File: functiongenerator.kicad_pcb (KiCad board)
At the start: 2 copper layers, 100 x 71 mm, 59 parts, among them J1 Conn_01x02_Socket, J2 Amplitude, J3 Amplitude, J4 offset, J5 offset, U1 LM6172, U2 LM6172, X1 CON1, X2 CON2

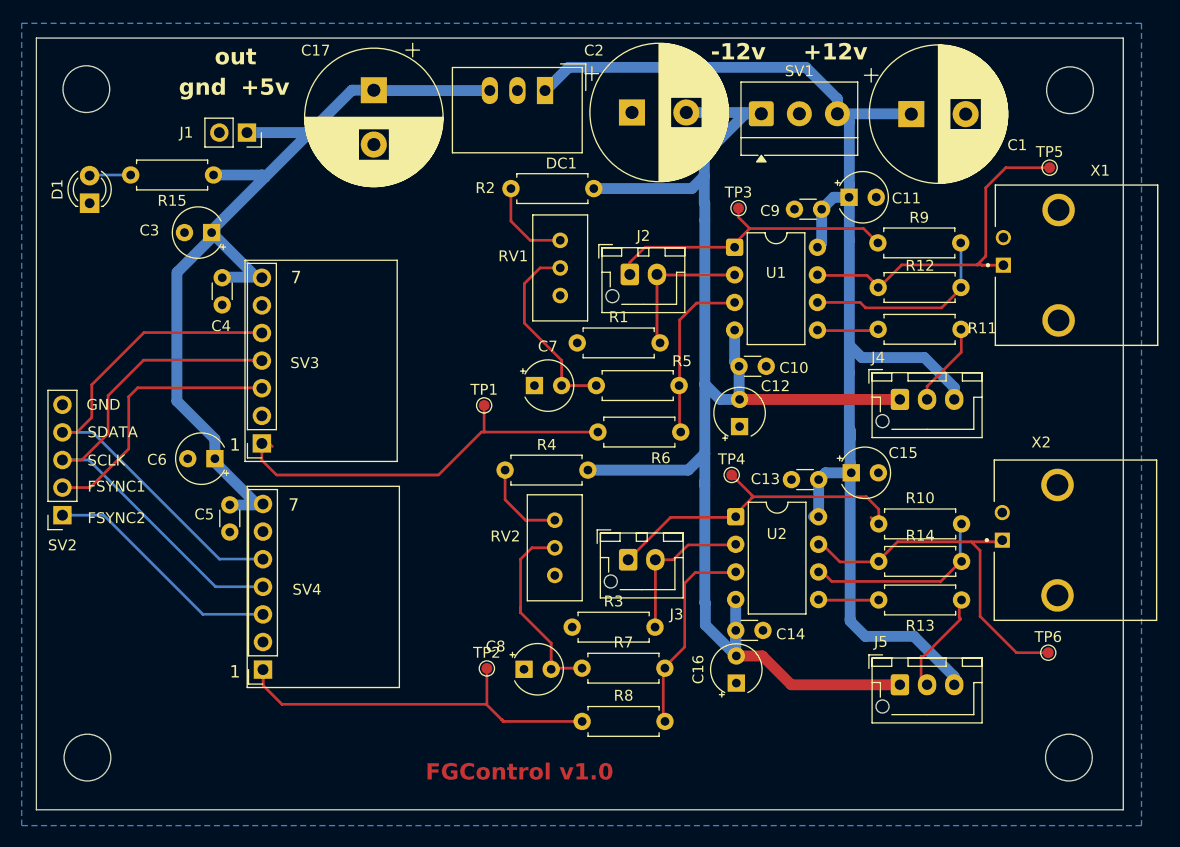
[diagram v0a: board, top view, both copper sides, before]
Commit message: first cleanup groundplane
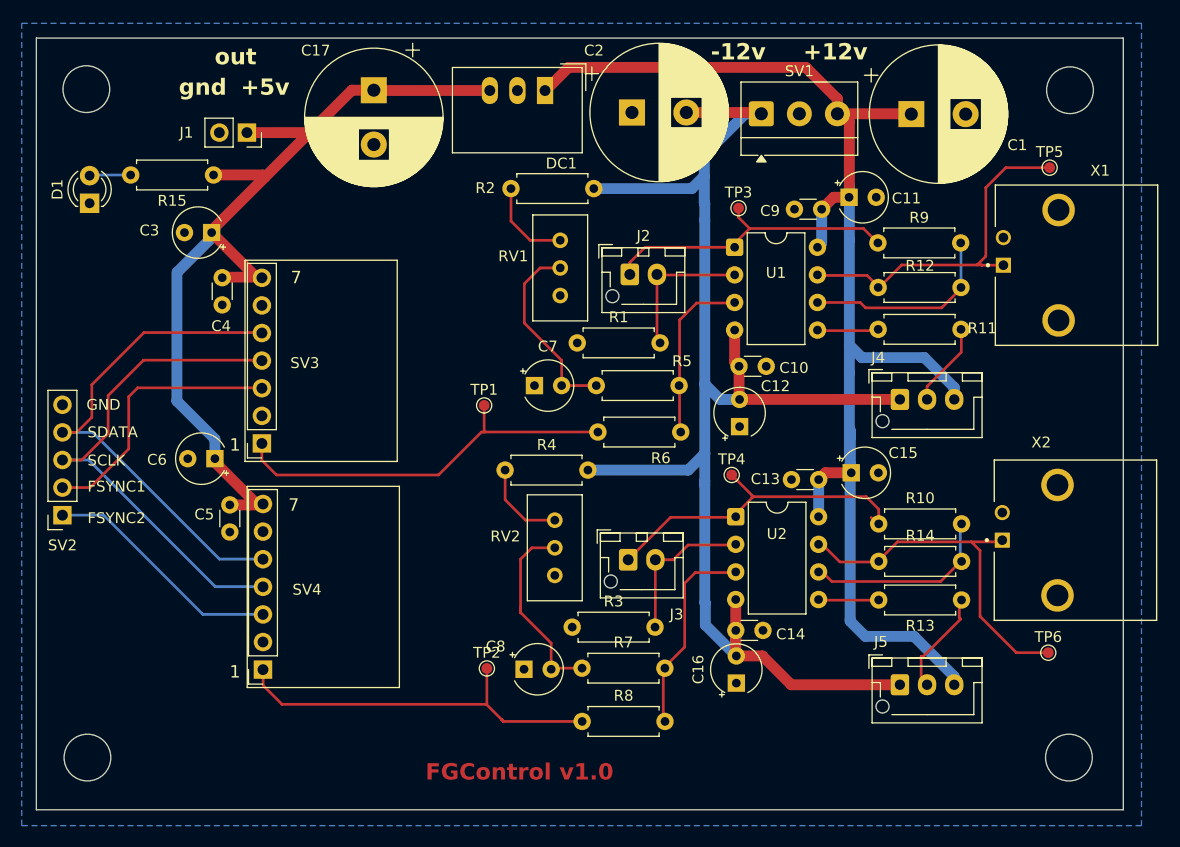
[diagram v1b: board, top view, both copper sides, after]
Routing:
- net /+12v: track 126.9 -> 131.7 mm
- net /+5v: track 84.5 -> 86.3 mm
- net Net-(SV3-Pin_1): track 38.1 -> 37.1 mm
- net /-12v: track 130.8 -> 131.4 mm

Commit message: moved offset potmeter connections
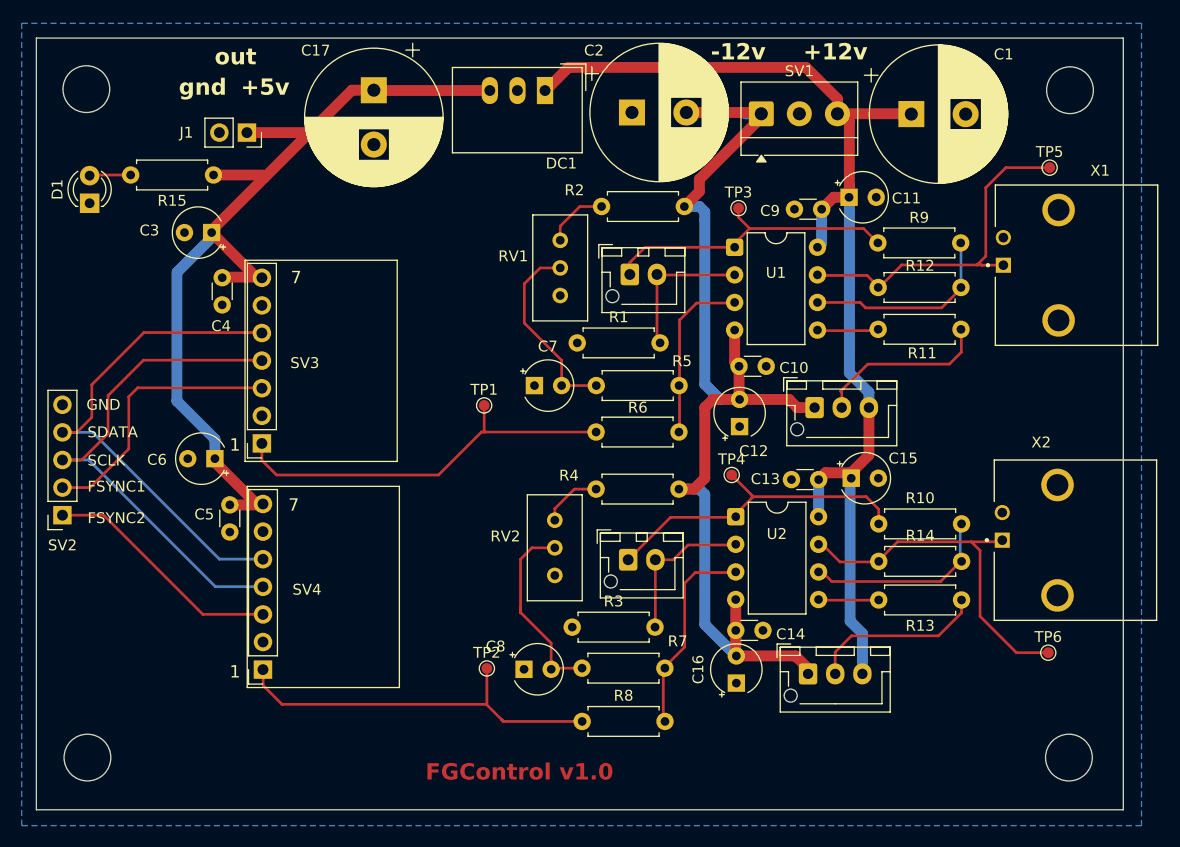
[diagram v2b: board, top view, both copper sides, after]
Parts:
- moved R4 8.56 mm to (157.6, 111.0)
- moved J5 8.51 mm to (169.5, 128.0)
- moved R2 8.50 mm to (158.1, 85.0)
- moved J4 7.89 mm to (170.1, 103.5)
- moved C15 0.50 mm to (173.5, 110.0)
- moved R6 0.16 mm to (150.0, 105.8)
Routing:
- net /-12v: track 131.4 -> 101.4 mm
- net /+12v: track 131.7 -> 109.7 mm
- net Net-(J4-Pin_2): track 7.57 -> 16.1 mm
- net Net-(J5-Pin_2): track 9.59 -> 16.3 mm
- net Net-(R4-Pad2): track 8.08 -> 5.61 mm
- net Net-(R2-Pad2): track 8.26 -> 5.86 mm
- net /+5v: track 86.3 -> 85.2 mm
- net Net-(J3-Pin_1): track 31.5 -> 30.7 mm

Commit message: removed exces traces
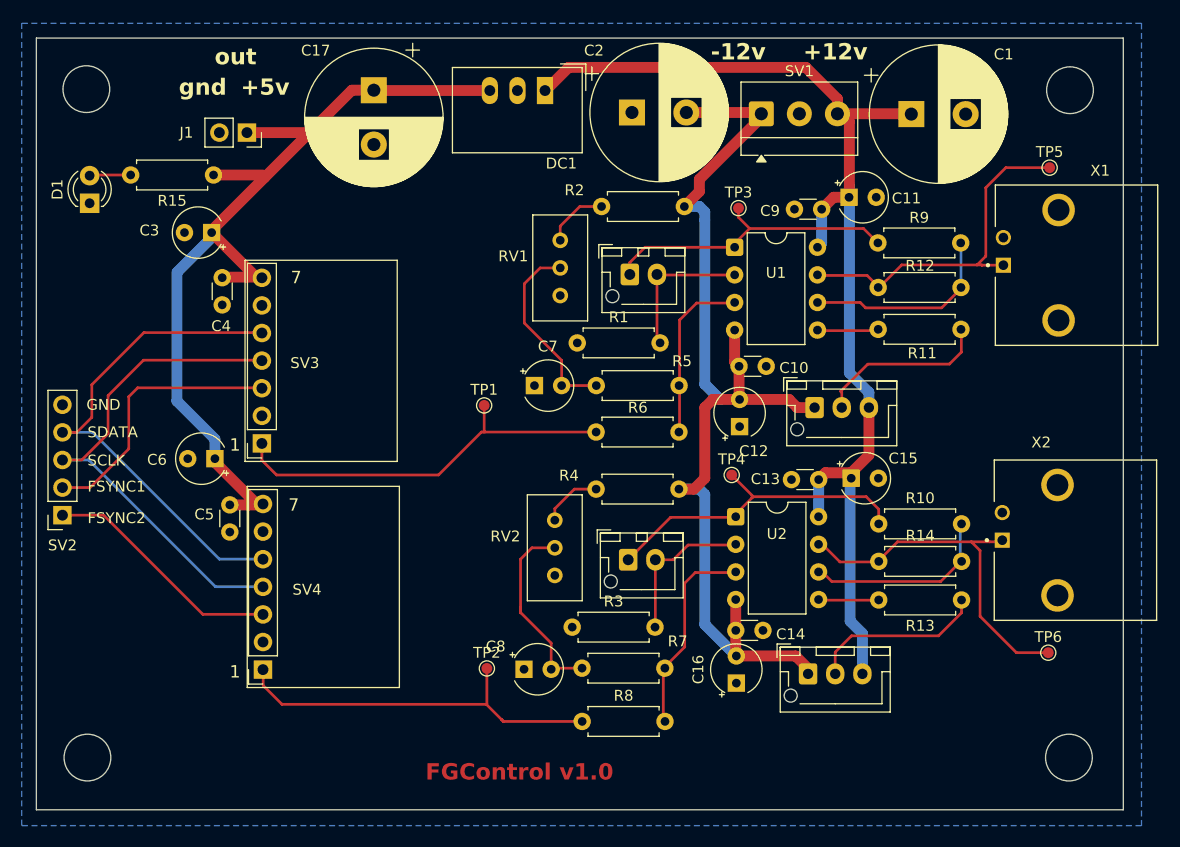
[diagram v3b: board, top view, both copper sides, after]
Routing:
- net /-12v: track 101.4 -> 98.0 mm
- net /+12v: track 109.7 -> 106.9 mm
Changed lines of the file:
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@@
-	)
-	(segment
-		(start 162.845 123.995)
-		(end 162.85 124)
-		(width 1)
-		(layer "B.Cu")
-		(net 16)
 	)
 	(segment
@@
 	)
 	(segment
-		(start 163.2 99.75)
-		(end 163.15 99.7)
-		(width 1)
-		(layer "B.Cu")
-		(net 16)
-	)
-	(segment
 		(start 158.12 85)
 		(end 159.5 85)
@@
 	)
 	(segment
-		(start 165.1325 76.4)
-		(end 165.2 76.4675)
-		(width 1)
-		(layer "B.Cu")
-		(net 16)
-	)
-	(segment
-		(start 162.745 99.295)
-		(end 163.15 99.7)
-		(width 1)
-		(layer "B.Cu")
-		(net 16)
-	)
-	(segment
-		(start 165.1675 76.5)
-		(end 165.2 76.4675)
-		(width 1)
-		(layer "B.Cu")
-		(net 16)
-	)
-	(segment
-		(start 165.2 76.4675)
-		(end 163.7325 76.4675)
-		(width 1)
-		(layer "B.Cu")
-		(net 16)
-	)
-	(segment
-		(start 162.85 124)
-		(end 162.85 125)
-		(width 1)
-		(layer "B.Cu")
-		(net 16)
-	)
-	(segment
 		(start 159.5 111)
 		(end 160 111.5)
@@
 	)
 	(segment
-		(start 165.0825 76.35)
-		(end 165.2 76.4675)
-		(width 1)
-		(layer "B.Cu")
-		(net 16)
-	)
-	(segment
 		(start 160 86.25)
 		(end 160 101.35)
@@
 	)
 	(segment
-		(start 129.58 74.33)
-		(end 129.55 74.3)
-		(width 1)
-		(layer "B.Cu")
-		(net 17)
-	)
-	(segment
 		(start 114.628856 87.871263)
 		(end 111.500059 91.000059)
@@
 	)
 	(segment
-		(start 129.35 74.55)
-		(end 129.05 74.25)
-		(width 1)
-		(layer "B.Cu")
-		(net 17)
-	)
-	(segment
 		(start 114.628856 87.4)
 		(end 114.628856 87.201144)
@@
 	)
 	(segment
-		(start 172.2 76.4675)
-		(end 172.5675 76.4675)
-		(width 1)
-		(layer "B.Cu")
-		(net 18)
-	)
-	(segment
 		(start 174.5 128)
 		(end 174.5 124.278856)
@@
 	)
 	(segment
-		(start 178.9675 76.4675)
-		(end 179 76.5)
-		(width 1)
-		(layer "B.Cu")
-		(net 18)
-	)
-	(segment
 		(start 170.75 85.25)
 		(end 170.75 88.365)
@@
 	)
 	(segment
-		(start 172.2 76.4675)
-		(end 172.2 75.1)
-		(width 1)
-		(layer "B.Cu")
-		(net 18)
-	)
-	(segment
 		(start 170.475 113.53)
 		(end 170.465 113.54)
@@
 		(width 1)
 		(layer "B.Cu")
-		(net 18)
-	)
-	(segment
-		(start 172.5675 76.4675)
-		(end 173.3 77.2)
-		(width 1)
-		(layer "B.Cu")

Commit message: more sparation between digital tracks channel 1
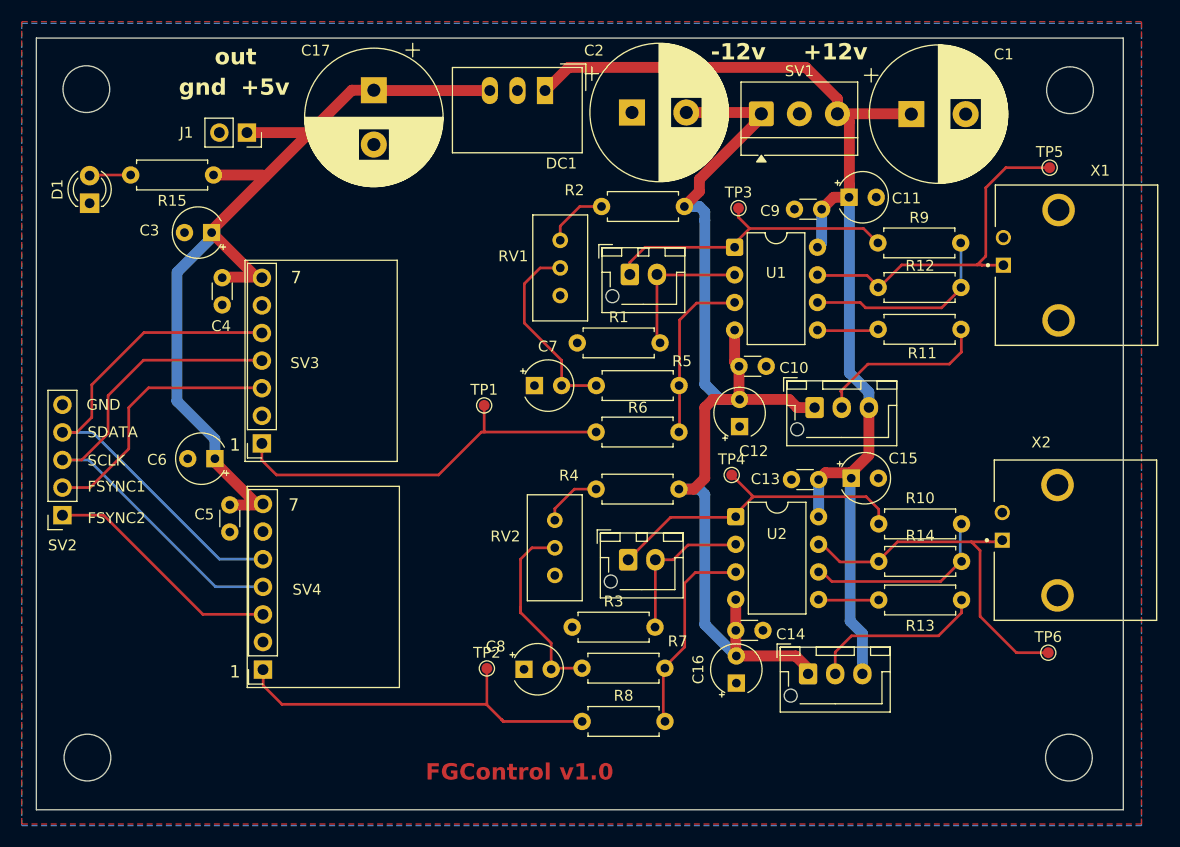
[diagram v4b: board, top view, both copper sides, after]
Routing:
- net Net-(SV2-Pin_2): track 25.0 -> 24.5 mm
- added copper zone on F.Cu, net GND
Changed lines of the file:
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@@
 			(layer "F.Fab")
 		)
-		(fp_text user "${REFERENCE}"
-			(at 3.81 0 0)
-			(layer "F.Fab")
-			(effects
-				(font
-					(size 1 1)
-					(thickness 0.15)
-				)
-			)
-		)
 		(pad "1" thru_hole circle
 			(at 0 0)
@@
 			(layer "F.Fab")
 		)
-		(fp_text user "${REFERENCE}"
-			(at 3.81 0 180)
-			(layer "F.Fab")
-			(effects
-				(font
-					(size 1 1)
-					(thickness 0.15)
-				)
-			)
-		)
 		(pad "1" thru_hole circle
 			(at 0 0 180)
@@
 	)
 	(segment
-		(start 103.36 110.86)
-		(end 100.9 110.86)
+		(start 119.3 101.68)
+		(end 108.82 101.68)
 		(width 0.25)
 		(layer "F.Cu")
@@
 	)
 	(segment
-		(start 119.3 101.68)
-		(end 107.82 101.68)
+		(start 103.36 110.86)
+		(end 100.9 110.86)
 		(width 0.25)
 		(layer "F.Cu")
@@
 	)
 	(segment
-		(start 107.82 101.68)
-		(end 107 102.5)
+		(start 103.4 110.9)
+		(end 103.36 110.86)
 		(width 0.25)
 		(layer "F.Cu")
@@
 	)
 	(segment
-		(start 107 102.5)
-		(end 107 107.3)
+		(start 107 107.3)
+		(end 103.4 110.9)
 		(width 0.25)
 		(layer "F.Cu")
@@
 	)
 	(segment
-		(start 103.4 110.9)
-		(end 103.36 110.86)
+		(start 108.82 101.68)
+		(end 107 103.5)
 		(width 0.25)
 		(layer "F.Cu")
@@
 	)
 	(segment
-		(start 107 107.3)
-		(end 103.4 110.9)
+		(start 107 103.5)
+		(end 107 107.3)
 		(width 0.25)
 		(layer "F.Cu")
@@
 		(net 1)
 		(net_name "GND")
+		(layer "F.Cu")
+		(name "GND")
+		(hatch edge 0.508)
+		(priority 6)
+		(connect_pads
+			(clearance 0.000001)
+		)
+		(min_thickness 0.0762)
+		(filled_areas_thickness no)
+		(fill yes
+			(thermal_gap 0.2024)
+			(thermal_bridge_width 0.2024)
+		)
+		(polygon
+			(pts
+				(xy 200.1773 141.8124) (xy 97.1549 141.8124) (xy 97.1549 68) (xy 200.1773 68)
+			)
+		)
+	)
+	(zone
+		(net 1)
+		(net_name "GND")
 		(layer "B.Cu")
 		(name "GND")
@@
 			(thermal_gap 0.2024)
 			(thermal_bridge_width 0.2024)
-			(island_removal_mode 1)
-			(island_area_min 10)
 		)
 		(polygon

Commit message: attached agnd to common gnd moved +5v connector to board edge
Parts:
- moved J1 3.90 mm to (117.9, 74.3)
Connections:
- SV3 pad 2: unconnected-(SV3-Pin_2-Pad2) -> GND
- SV4 pad 2: unconnected-(SV4-Pin_2-Pad2) -> GND
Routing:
- net /+5v: track 84.8 -> 90.7 mm
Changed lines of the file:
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@@
 	(net 26 "Net-(SV3-Pin_1)")
 	(net 27 "Net-(SV4-Pin_1)")
-	(net 28 "unconnected-(SV3-Pin_2-Pad2)")
-	(net 29 "unconnected-(SV4-Pin_2-Pad2)")
-	(net 30 "Net-(R4-Pad2)")
-	(net 31 "Net-(R14-Pad1)")
+	(net 28 "Net-(R4-Pad2)")
+	(net 29 "Net-(R14-Pad1)")
 	(footprint "Resistor_THT:R_Axial_DIN0207_L6.3mm_D2.5mm_P7.62mm_Horizontal"
 		(layer "F.Cu")
@@
 			(size 1 1)
 			(layers "F.Cu" "F.Mask")
-			(net 31 "Net-(R14-Pad1)")
+			(net 29 "Net-(R14-Pad1)")
 			(pinfunction "1")
 			(pintype "passive")
@@
 			(layers "*.Cu" "*.Mask")
 			(remove_unused_layers no)
-			(net 31 "Net-(R14-Pad1)")
+			(net 29 "Net-(R14-Pad1)")
 			(pintype "passive")
 			(solder_mask_margin 0.102)
@@
 			(layers "*.Cu" "*.Mask")
 			(remove_unused_layers no)
-			(net 30 "Net-(R4-Pad2)")
+			(net 28 "Net-(R4-Pad2)")
 			(pinfunction "3")
 			(pintype "passive")
@@
 			(layers "*.Cu" "*.Mask")
 			(remove_unused_layers no)
-			(net 31 "Net-(R14-Pad1)")
+			(net 29 "Net-(R14-Pad1)")
 			(pintype "output")
 		)
@@
 			(layers "*.Cu" "*.Mask")
 			(remove_unused_layers no)
-			(net 29 "unconnected-(SV4-Pin_2-Pad2)")
+			(net 1 "GND")
 			(pinfunction "Pin_2")
-			(pintype "passive+no_connect")
+			(pintype "passive")
 		)
 		(pad "3" thru_hole circle
@@
 			(layers "*.Cu" "*.Mask")
 			(remove_unused_layers no)
-			(net 31 "Net-(R14-Pad1)")
+			(net 29 "Net-(R14-Pad1)")
 			(pintype "passive")
 		)
@@
 			(layer "F.CrtYd")
 		)
-		(fp_text user "${REFERENCE}"
-			(at 0 -3.048856 0)
-			(layer "F.Fab")
-			(effects
-				(font
-					(size 1 1)
-					(thickness 0.15)
-				)
-			)
-		)
 		(pad "" np_thru_hole circle
 			(at 0 0)
@@
 	(footprint "Connector_PinSocket_2.54mm:PinSocket_1x02_P2.54mm_Vertical"
 		(layer "F.Cu")
-		(at 117.875 78.2 -90)
+		(at 117.875 74.3 -90)
 		(descr "Through hole straight socket strip, 1x02, 2.54mm pitch, single row (from Kicad 4.0.7), script generated")
 		(tags "Through hole socket strip THT 1x02 2.54mm single row")
@@
 			(layers "*.Cu" "*.Mask")
 			(remove_unused_layers no)
-			(net 28 "unconnected-(SV3-Pin_2-Pad2)")
+			(net 1 "GND")
 			(pinfunction "Pin_2")
-			(pintype "passive+no_connect")
+			(pintype "passive")
 		)
 		(pad "3" thru_hole circle
@@
 			(layers "*.Cu" "*.Mask")
 			(remove_unused_layers no)
-			(net 30 "Net-(R4-Pad2)")
+			(net 28 "Net-(R4-Pad2)")
 			(pintype "passive")
 		)
@@
 	)
 	(gr_text "+5v"
-		(at 117.3 74.9 0)
+		(at 117.3 71.5 0)
 		(layer "F.SilkS")
 		(effects
@@
 	)
 	(gr_text "out"
-		(at 114.9 72.1 0)
+		(at 114.5 78 0)
 		(layer "F.SilkS")
 		(effects
@@
 	)
 	(gr_text "gnd"
-		(at 111.6 74.9 0)
+		(at 111.6 71.5 0)
 		(layer "F.SilkS")
 		(effects
@@
 	)
 	(segment
-		(start 117.875 78.2)
-		(end 123.63 78.2)
-		(width 1)
-		(layer "F.Cu")
-		(net 17)
-	)
-	(segment
 		(start 118.09 112.37)
 		(end 118 112.46)
@@
 	)
 	(segment
+		(start 129.55 74.3)
+		(end 117.875 74.3)
+		(width 1)
+		(layer "F.Cu")
+		(net 17)
+	)
+	(segment
 		(start 118.748856 91.52)
 		(end 114.628856 87.4)
@@
 		(width 0.25)
 		(layer "F.Cu")
-		(net 30)
+		(net 28)
 	)
 	(segment
@@
 		(width 0.25)
 		(layer "F.Cu")
-		(net 30)
+		(net 28)
 	)
 	(segment
@@
 		(width 0.25)
 		(layer "F.Cu")
-		(net 30)
+		(net 28)
 	)
 	(segment
@@
 		(width 0.25)
 		(layer "F.Cu")
-		(net 31)
+		(net 29)
 	)
 	(segment
@@
 		(width 0.25)
 		(layer "F.Cu")
-		(net 31)
+		(net 29)
 	)
 	(segment
@@
 		(width 0.25)
 		(layer "F.Cu")
-		(net 31)
+		(net 29)
 	)
 	(segment
@@
 		(width 0.25)
 		(layer "F.Cu")
-		(net 31)
+		(net 29)
 	)
 	(segment
@@
 		(width 0.25)
 		(layer "F.Cu")
-		(net 31)
+		(net 29)
 	)
 	(segment
@@
 		(width 0.25)
 		(layer "F.Cu")
-		(net 31)
+		(net 29)
 	)
 	(segment
@@
 		(width 0.25)
 		(layer "F.Cu")
-		(net 31)
+		(net 29)
 	)
 	(segment
@@
 		(width 0.25)
 		(layer "F.Cu")
-		(net 31)
+		(net 29)
 	)
 	(segment
@@
 		(width 0.25)
 		(layer "F.Cu")
-		(net 31)
+		(net 29)
 	)
 	(segment
@@
 		(width 0.25)
 		(layer "F.Cu")
-		(net 31)
+		(net 29)
 	)
 	(zone

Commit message: seperated channels more updated label to v1.1
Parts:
- J2, J3: footprint Connector_JST:JST_XH_B2B-XH-AM_1x02_P2.50mm_Vertical -> Connector_JST:JST_XH_B2B-XH-A_1x02_P2.50mm_Vertical
- J4, J5: footprint Connector_JST:JST_XH_B3B-XH-AM_1x03_P2.50mm_Vertical -> Connector_JST:JST_XH_B3B-XH-A_1x03_P2.50mm_Vertical
- SV1: footprint TerminalBlock_MetzConnect:TerminalBlock_MetzConnect_Type059_RT06303HBWC_1x03_P3.50mm_Horizontal -> TerminalBlock_Phoenix:TerminalBlock_Phoenix_PT-1,5-3-3.5-H_1x03_P3.50mm_Horizontal
- moved SV1 7.30 mm to (172.5, 76.5), turned to 180 degrees
- moved C8 4.23 mm to (143.4, 131.8)
- moved RV2 4.23 mm to (146.2, 123.2)
- moved C13 4.22 mm to (170.5, 114.3)
- moved C14 4.22 mm to (162.8, 128.2)
- moved C16 4.22 mm to (162.9, 133.1)
- moved J3 4.22 mm to (152.9, 121.7)
- moved J5 4.22 mm to (169.5, 132.2)
- moved R13 4.22 mm to (183.6, 125.4)
- moved R14 4.22 mm to (176.0, 121.9)
- moved R3 4.22 mm to (147.8, 127.9)
- moved R4 4.22 mm to (157.6, 115.2)
- moved R7 4.22 mm to (148.7, 131.7)
- moved R8 4.22 mm to (148.7, 136.6)
- moved TP4 4.22 mm to (162.5, 113.9)
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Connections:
- SV1 pad 1: /-12v -> /+12v
- SV1 pad 3: /+12v -> /-12v
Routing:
- net Net-(SV4-Pin_1): track 35.8 -> 41.8 mm
- net /-12v: track 98.0 -> 102.2 mm
- net /+12v: track 106.9 -> 110.0 mm
- net Net-(J2-Pin_1): track 30.2 -> 28.5 mm
- net Net-(SV3-Pin_1): track 37.1 -> 36.1 mm
- net Net-(U2B--): track 17.2 -> 18.1 mm
- net Net-(J2-Pin_2): track 14.1 -> 13.6 mm
- removed copper zone on B.Cu, net GND
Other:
- board text added: "FGControl v1.1"
- board text removed: "FGControl v1.0"
